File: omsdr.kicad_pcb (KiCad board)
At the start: 2 copper layers, 50 x 50 mm, 55 parts, among them J1 I/Q Out, J2 ANT, J3 ISP, J4 LO, J8 PWR, SW1 SW_SPST, SW2 SW_SPST, T1 CX2074NL, U1 LT6231, U2 FST3253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

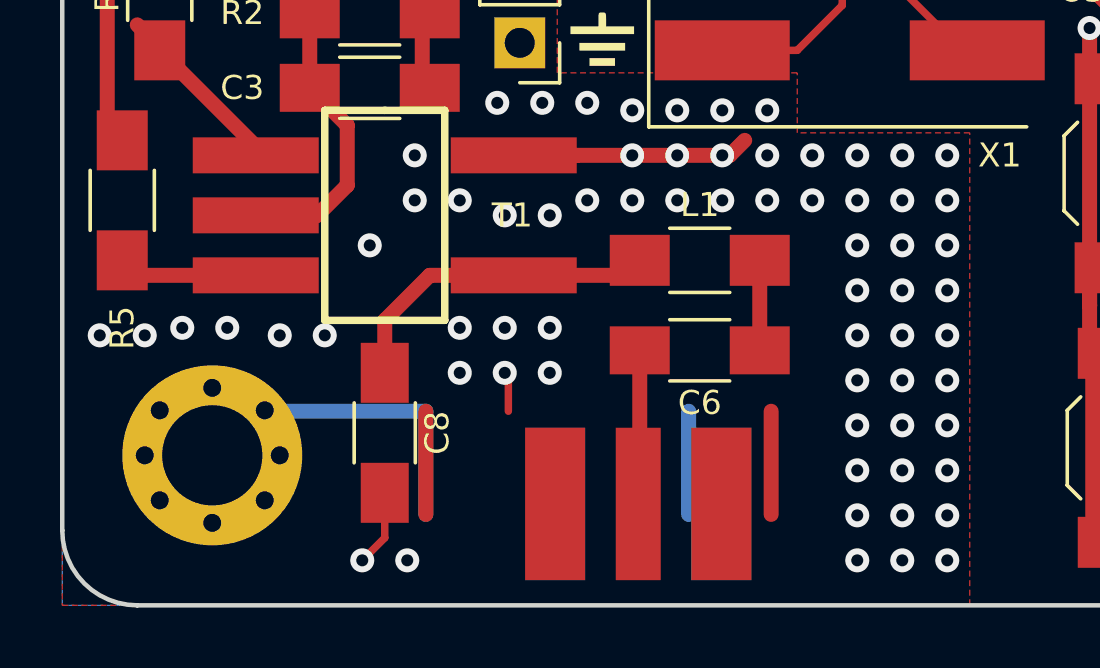
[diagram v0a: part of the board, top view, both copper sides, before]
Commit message: Reworked input bandpass filter
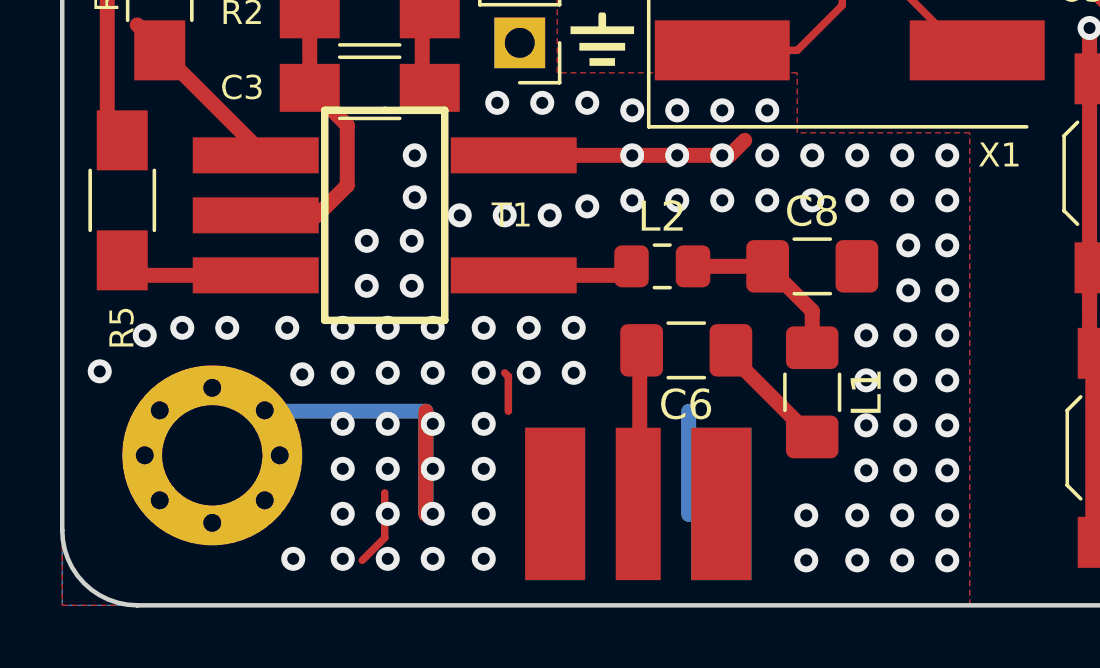
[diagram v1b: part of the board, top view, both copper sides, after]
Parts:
- added L2: 0.56u, Inductor_SMD:L_0805_2012Metric_Pad1.15x1.40mm_HandSolder, F.Cu at (120.0, 88.7)
- C6: footprint Capacitors_SMD:C_1206_HandSoldering -> Capacitor_SMD:C_1206_3216Metric_Pad1.42x1.75mm_HandSolder
- C8: value 1500p -> 680p; footprint Capacitors_SMD:C_1206_HandSoldering -> Capacitor_SMD:C_1206_3216Metric_Pad1.42x1.75mm_HandSolder
- L1: footprint Resistors_SMD:R_1206_HandSoldering -> Inductor_SMD:L_1206_3216Metric_Pad1.42x1.75mm_HandSolder
- moved C8 15.3 mm to (125.0, 88.7), turned to 0 degrees
- moved L1 5.78 mm to (125.0, 92.9), turned to 270 degrees
- moved C6 0.45 mm to (120.8, 91.5)
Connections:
- T1 pad 2: Net-(C8-Pad1) -> Net-(L2-Pad1)
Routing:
- net Net-(L2-Pad1): track 0.00 -> 5.55 mm
- net Net-(C8-Pad1): track 10.8 -> 5.82 mm
- net GND: track 136.1 -> 132.7 mm, vias 82 -> 106
- net Net-(C6-Pad1): track 3.00 -> 4.02 mm
- net Net-(C6-Pad2): track 5.68 -> 4.97 mm

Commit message: Updated copyright dates
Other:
- board text added: "Based on work by Tony Parks (c) 2017,18,19 CC-BY-SA"
- board text added: "by Matt Weyland (HB9FRV) and Peter Klaentschi (HB9GHY)"
- board text removed: "(c) 2017 by Matt Weyland (HB9FRV) and Peter Klaentschi (HB9GHY)"
- board text removed: "Based on work by Tony Parks (c) 2017, CC-BY-SA PCB fulfilled by Hackvana"
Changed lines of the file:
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@@
   )
   (setup
-    (last_trace_width 0.5)
+    (last_trace_width 0.25)
     (user_trace_width 0.5)
     (trace_clearance 0.15)
@@
     (effects (font (size 1.5 1.5) (thickness 0.3)))
   )
-  (gr_text "Based on work by Tony Parks\n(c) 2017, CC-BY-SA\nPCB fulfilled by Hackvana" (at 147.25 89.25) (layer B.SilkS)
+  (gr_text "Based on work by Tony Parks\n(c) 2017,18,19 CC-BY-SA" (at 147.25 89.25) (layer B.SilkS)
     (effects (font (size 0.75 0.75) (thickness 0.15)) (justify left mirror))
   )
-  (gr_text "(c) 2017 by Matt Weyland (HB9FRV)\nand Peter Klaentschi (HB9GHY)" (at 147.5 85) (layer B.SilkS)
+  (gr_text "by Matt Weyland (HB9FRV)\nand Peter Klaentschi (HB9GHY)" (at 147.5 85) (layer B.SilkS)
     (effects (font (size 1 1) (thickness 0.2)) (justify left mirror))
   )

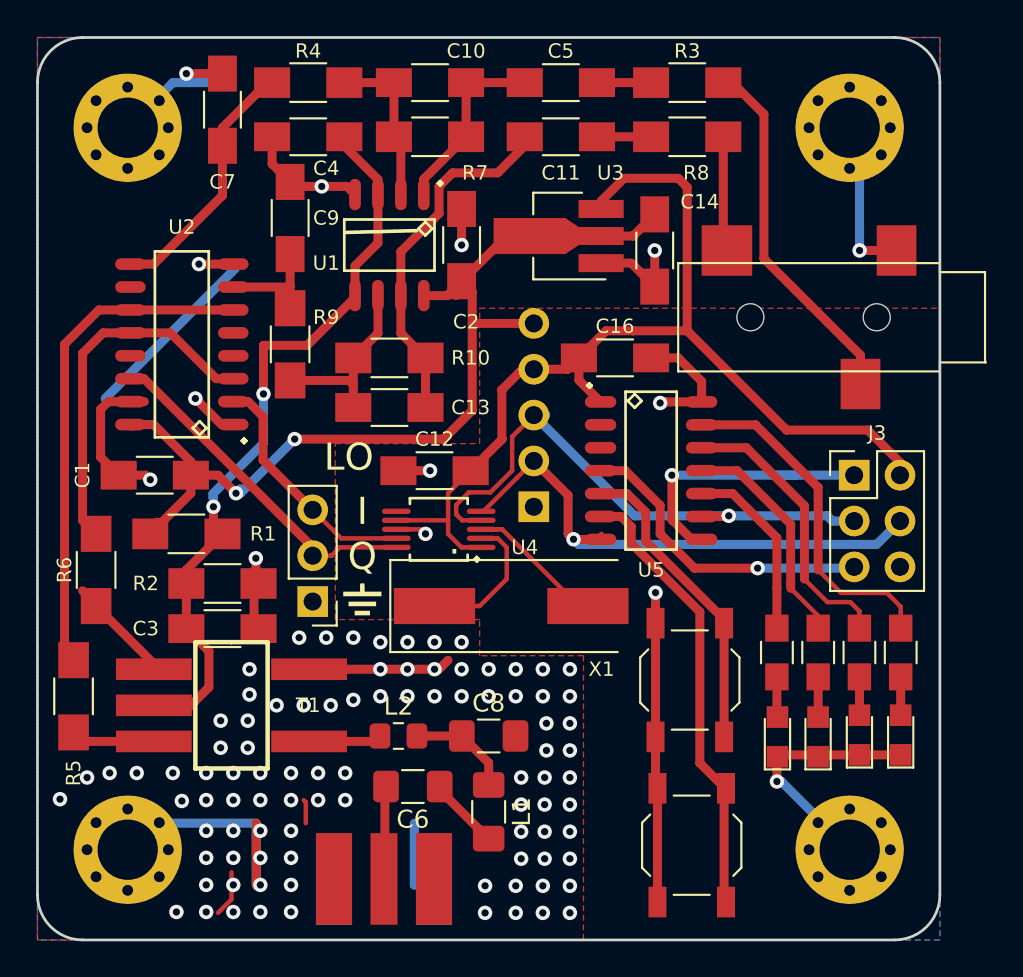
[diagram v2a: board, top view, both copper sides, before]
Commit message: Replaced footprints with versions from new kicad footprint library
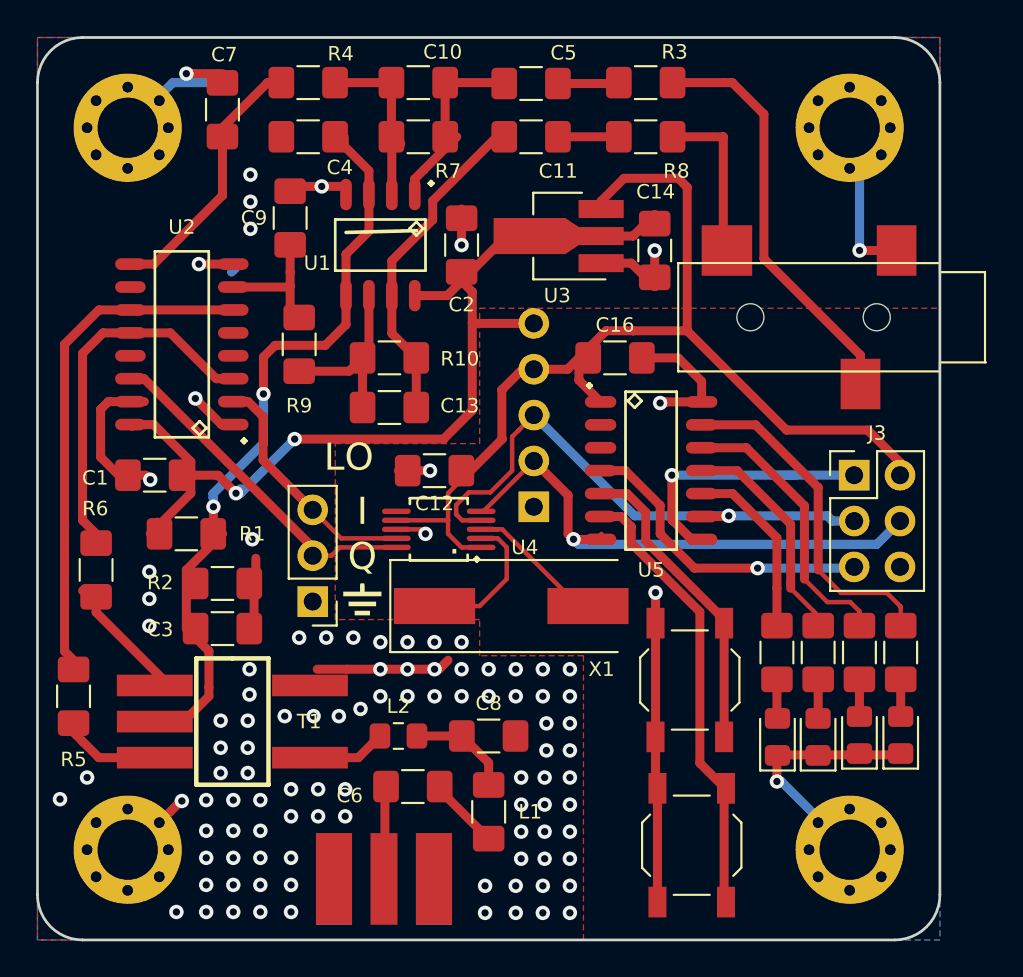
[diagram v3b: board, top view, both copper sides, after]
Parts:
- C1, C10, C11, C12, C13, C14, C16, C2, C3, C4, C5, C7, C9: footprint Capacitors_SMD:C_1206_HandSoldering -> Capacitor_SMD:C_1206_3216Metric_Pad1.42x1.75mm_HandSolder
- D1, D2, D3, D4: footprint LEDs:LED_0805 -> LED_SMD:LED_0805_2012Metric_Pad1.15x1.40mm_HandSolder
- R1, R10, R2, R3, R4, R5, R6, R7, R8, R9: footprint Resistors_SMD:R_1206_HandSoldering -> Resistor_SMD:R_1206_3216Metric_Pad1.42x1.75mm_HandSolder
- R11, R12, R13, R14: footprint Resistors_SMD:R_0805_HandSoldering -> Resistor_SMD:R_1206_3216Metric_Pad1.42x1.75mm_HandSolder
- U3: footprint TO_SOT_Packages_SMD:SOT-89-3_Handsoldering -> Package_TO_SOT_SMD:SOT-89-3_Handsoldering
- moved R3 2.30 mm to (133.7, 52.5)
- moved R8 2.30 mm to (133.7, 55.5)
- moved C5 1.65 mm to (127.3, 52.5)
- moved C11 1.65 mm to (127.3, 55.5)
- moved T1 0.90 mm to (110.8, 87.9)
- moved C10 0.65 mm to (121.1, 52.5)
- moved R7 0.65 mm to (121.1, 55.5)
- moved R9 0.50 mm to (114.5, 67.0)
- moved U1 0.50 mm to (119.0, 61.5)
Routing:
- net GND: track 132.7 -> 99.6 mm, vias 106 -> 107
- net Net-(J1-Pad2): track 20.1 -> 23.0 mm
- net Net-(J1-Pad1): track 6.38 -> 9.20 mm
- net Net-(C11-Pad1): track 20.4 -> 18.4 mm
- net Net-(C9-Pad1): track 5.83 -> 7.41 mm
- net /Vhalf: track 42.0 -> 43.4 mm
- net Net-(R5-Pad2): track 5.81 -> 6.58 mm
- net Net-(L2-Pad1): track 5.55 -> 6.30 mm
- net Net-(C10-Pad2): track 11.2 -> 10.5 mm
- net Net-(R6-Pad2): track 8.61 -> 8.00 mm

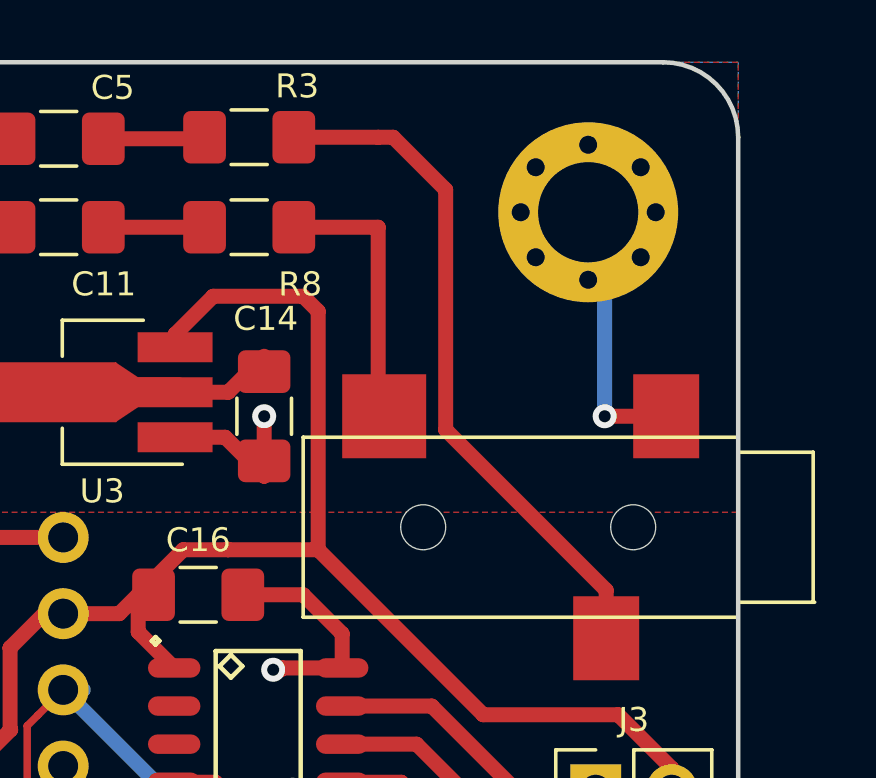
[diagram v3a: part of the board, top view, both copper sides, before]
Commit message: Adding pin header for IQ audio tap
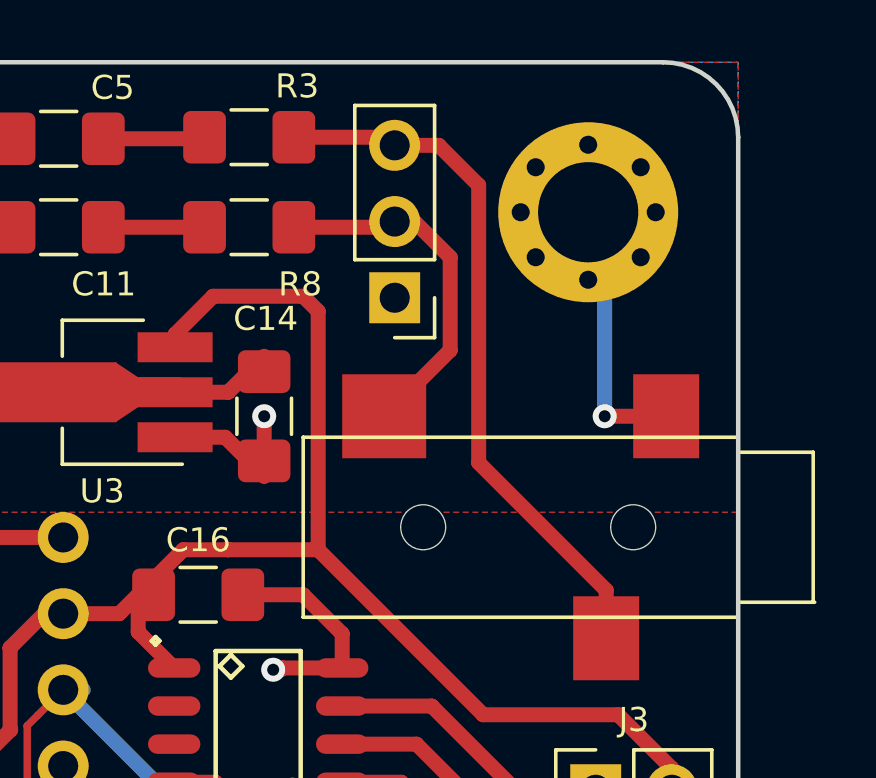
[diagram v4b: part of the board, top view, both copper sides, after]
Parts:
- added J5: I/Q Out, Connector_PinHeader_2.54mm:PinHeader_1x03_P2.54mm_Vertical, F.Cu at (138.6, 57.9)
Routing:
- net Net-(J1-Pad1): track 9.20 -> 12.3 mm
- net Net-(J1-Pad2): track 23.0 -> 24.2 mm
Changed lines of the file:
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@@
     (thickness 1.6)
     (drawings 170)
-    (tracks 447)
+    (tracks 453)
     (zones 0)
-    (modules 56)
+    (modules 57)
     (nets 48)
   )
@@
     (add_net "Net-(U5-Pad2)")
     (add_net "Net-(U5-Pad3)")
+  )
+  (module Connector_PinHeader_2.54mm:PinHeader_1x03_P2.54mm_Vertical (layer F.Cu)
+    (at 138.55 57.85 180)
+    (descr "Through hole straight pin header, 1x03, 2.54mm pitch, single row")
+    (tags "Through hole pin header THT 1x03 2.54mm single row")
+    (fp_text reference J5 (at 0 -2.33 180) (layer F.SilkS) hide
+      (effects (font (size 1 1) (thickness 0.15)))
+    )
+    (fp_text value "I/Q Out" (at 0 7.41 180) (layer F.Fab)
+      (effects (font (size 1 1) (thickness 0.15)))
+    )
+    (fp_line (start -0.635 -1.27) (end 1.27 -1.27) (layer F.Fab) (width 0.1))
+    (fp_line (start 1.27 -1.27) (end 1.27 6.35) (layer F.Fab) (width 0.1))
+    (fp_line (start 1.27 6.35) (end -1.27 6.35) (layer F.Fab) (width 0.1))
+    (fp_line (start -1.27 6.35) (end -1.27 -0.635) (layer F.Fab) (width 0.1))
+    (fp_line (start -1.27 -0.635) (end -0.635 -1.27) (layer F.Fab) (width 0.1))
+    (fp_line (start -1.33 6.41) (end 1.33 6.41) (layer F.SilkS) (width 0.12))
+    (fp_line (start -1.33 1.27) (end -1.33 6.41) (layer F.SilkS) (width 0.12))
+    (fp_line (start 1.33 1.27) (end 1.33 6.41) (layer F.SilkS) (width 0.12))
+    (fp_line (start -1.33 1.27) (end 1.33 1.27) (layer F.SilkS) (width 0.12))
+    (fp_line (start -1.33 0) (end -1.33 -1.33) (layer F.SilkS) (width 0.12))
+    (fp_line (start -1.33 -1.33) (end 0 -1.33) (layer F.SilkS) (width 0.12))
+    (fp_line (start -1.8 -1.8) (end -1.8 6.85) (layer F.CrtYd) (width 0.05))
+    (fp_line (start -1.8 6.85) (end 1.8 6.85) (layer F.CrtYd) (width 0.05))
+    (fp_line (start 1.8 6.85) (end 1.8 -1.8) (layer F.CrtYd) (width 0.05))
+    (fp_line (start 1.8 -1.8) (end -1.8 -1.8) (layer F.CrtYd) (width 0.05))
+    (fp_text user %R (at 0 2.54 270) (layer F.Fab)
+      (effects (font (size 1 1) (thickness 0.15)))
+    )
+    (pad 1 thru_hole rect (at 0 0 180) (size 1.7 1.7) (drill 1) (layers *.Cu *.Mask)
+      (net 2 GND))
+    (pad 2 thru_hole oval (at 0 2.54 180) (size 1.7 1.7) (drill 1) (layers *.Cu *.Mask)
+      (net 12 "Net-(J1-Pad1)"))
+    (pad 3 thru_hole oval (at 0 5.08 180) (size 1.7 1.7) (drill 1) (layers *.Cu *.Mask)
+      (net 8 "Net-(J1-Pad2)"))
+    (model ${KISYS3DMOD}/Connector_PinHeader_2.54mm.3dshapes/PinHeader_1x03_P2.54mm_Vertical.wrl
+      (at (xyz 0 0 0))
+      (scale (xyz 1 1 1))
+      (rotate (xyz 0 0 0))
+    )
   )
   (module Package_TO_SOT_SMD:SOT-89-3_Handsoldering (layer F.Cu)
@@
   (segment (start 132.1625 52.55) (end 132.2125 52.5) (width 0.5) (layer F.Cu) (net 7))
   (segment (start 128.8375 52.55) (end 132.1625 52.55) (width 0.5) (layer F.Cu) (net 7))
-  (segment (start 140.25 62.25) (end 145.6 67.6) (width 0.5) (layer F.Cu) (net 8))
   (segment (start 145.6 67.6) (end 145.6 69.2) (width 0.5) (layer F.Cu) (net 8))
-  (segment (start 140.25 54.25) (end 140.25 62.25) (width 0.5) (layer F.Cu) (net 8))
-  (segment (start 138.5 52.5) (end 140.25 54.25) (width 0.5) (layer F.Cu) (net 8))
   (segment (start 138 52.5) (end 138.5 52.5) (width 0.5) (layer F.Cu) (net 8))
-  (segment (start 138 52.5) (end 135.1875 52.5) (width 0.5) (layer F.Cu) (net 8))
+  (segment (start 138.28 52.5) (end 138.55 52.77) (width 0.5) (layer F.Cu) (net 8))
+  (segment (start 135.1875 52.5) (end 138.28 52.5) (width 0.5) (layer F.Cu) (net 8))
+  (segment (start 138.55 52.77) (end 140.02 52.77) (width 0.5) (layer F.Cu) (net 8))
+  (segment (start 140.02 52.77) (end 141.35 54.1) (width 0.5) (layer F.Cu) (net 8))
+  (segment (start 141.35 54.1) (end 141.35 63.35) (width 0.5) (layer F.Cu) (net 8))
+  (segment (start 141.35 63.35) (end 145.6 67.6) (width 0.5) (layer F.Cu) (net 8))
   (segment (start 119.635 62.365) (end 119.635 64.3) (width 0.5) (layer F.Cu) (net 9))
   (segment (start 121.9 60.1) (end 119.635 62.365) (width 0.5) (layer F.Cu) (net 9))
@@
   (segment (start 114 65.0125) (end 114.5 65.5125) (width 0.5) (layer F.Cu) (net 11))
   (segment (start 114 63.75) (end 114 65.0125) (width 0.5) (layer F.Cu) (net 11))
-  (segment (start 138 55.5) (end 138 61.6) (width 0.5) (layer F.Cu) (net 12))
   (segment (start 138 61.6) (end 138.2 61.8) (width 0.5) (layer F.Cu) (net 12))
-  (segment (start 138 55.5) (end 135.1875 55.5) (width 0.5) (layer F.Cu) (net 12))
+  (segment (start 138.36 55.5) (end 138.55 55.31) (width 0.5) (layer F.Cu) (net 12))
+  (segment (start 135.1875 55.5) (end 138.36 55.5) (width 0.5) (layer F.Cu) (net 12))
+  (segment (start 138.55 55.31) (end 139.21 55.31) (width 0.5) (layer F.Cu) (net 12))
+  (segment (start 139.21 55.31) (end 140.4 56.5) (width 0.5) (layer F.Cu) (net 12))
+  (segment (start 140.4 59.6) (end 138.2 61.8) (width 0.5) (layer F.Cu) (net 12))
+  (segment (start 140.4 56.5) (end 140.4 59.6) (width 0.5) (layer F.Cu) (net 12))
   (segment (start 128.8375 55.5) (end 132.2125 55.5) (width 0.5) (layer F.Cu) (net 13))
   (segment (start 120.135 55.885) (end 119.75 55.5) (width 0.5) (layer F.Cu) (net 14))
